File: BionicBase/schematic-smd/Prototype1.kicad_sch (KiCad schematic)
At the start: 11 parts, among them J1 Bionic_ZIF_Socket_48pin, SW1 Tact_SW, U1 TXS0108EPW, U2 TXS0108EPW, U3 TXS0108EPW, U4 TXS0108EPW, U5 TXS0108EPW

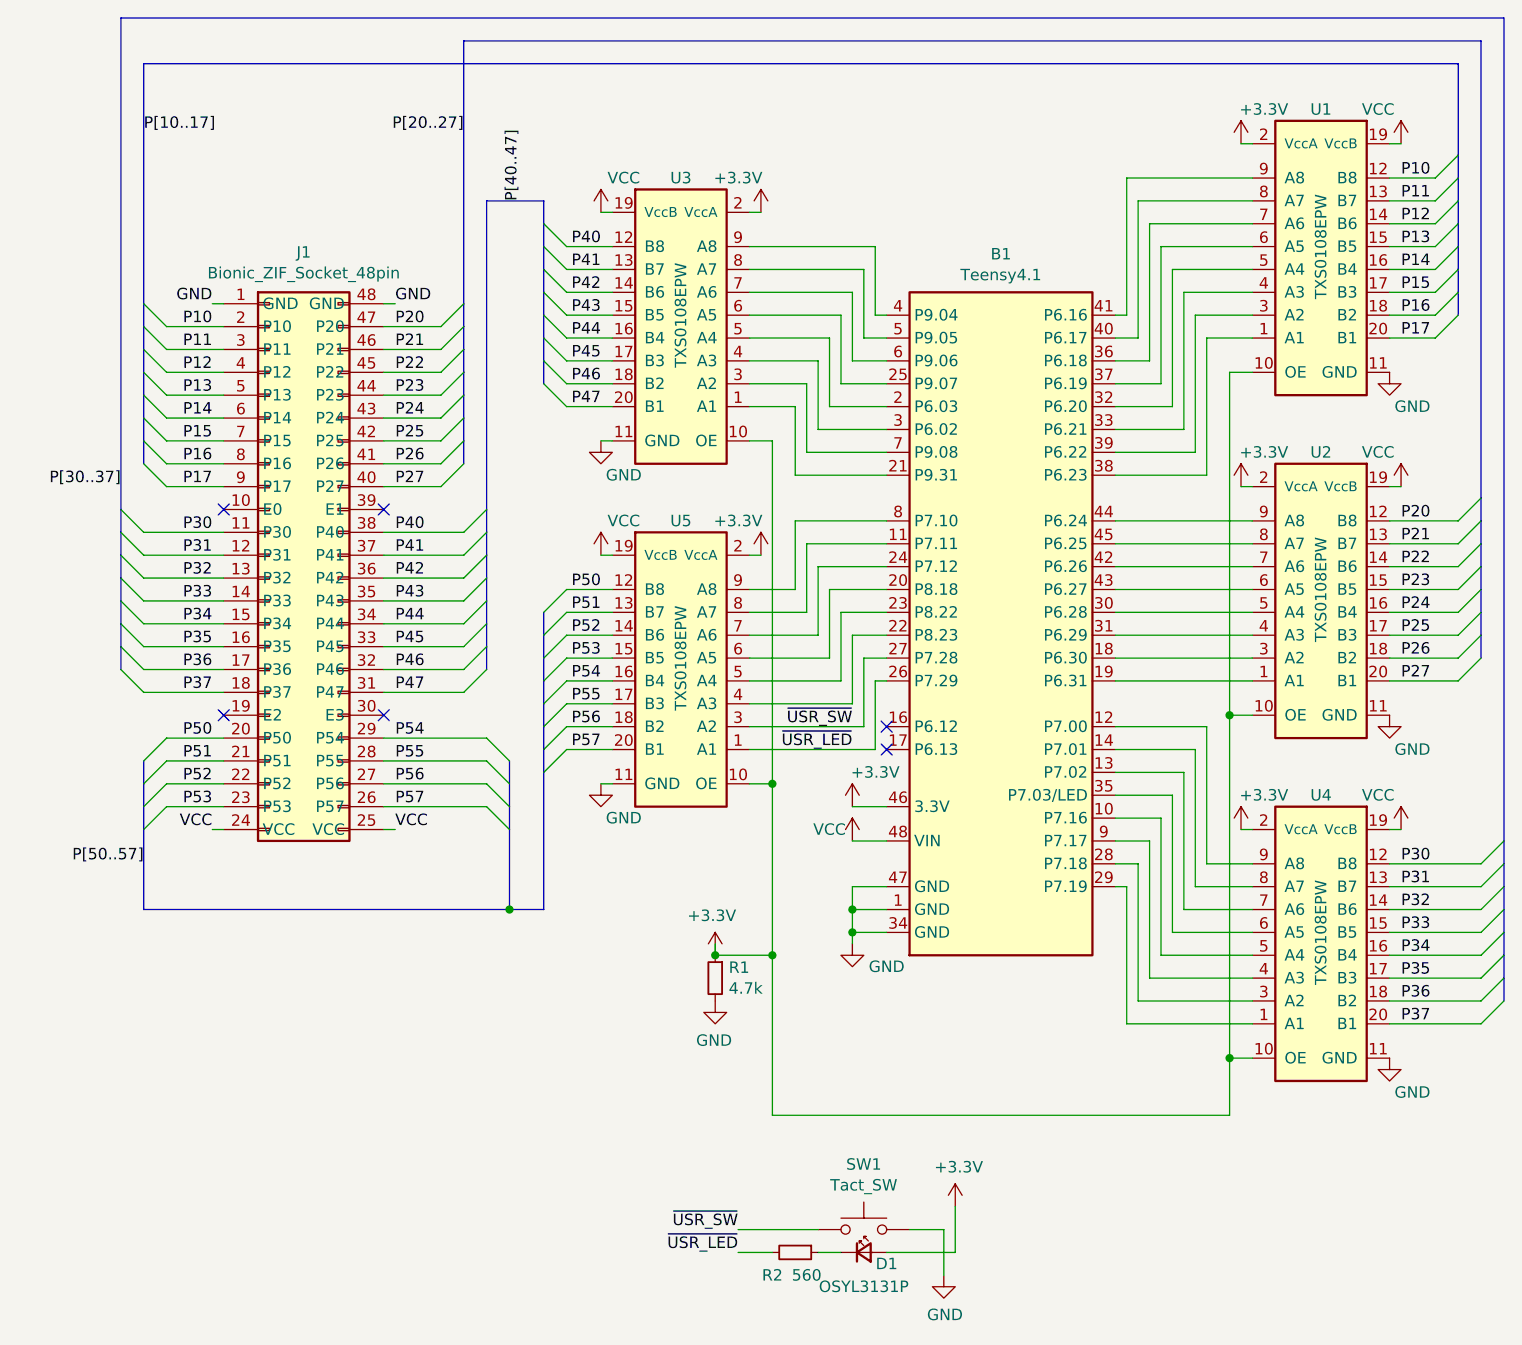
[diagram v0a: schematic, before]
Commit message: [BionicBase] Add schematics using surface mount devices
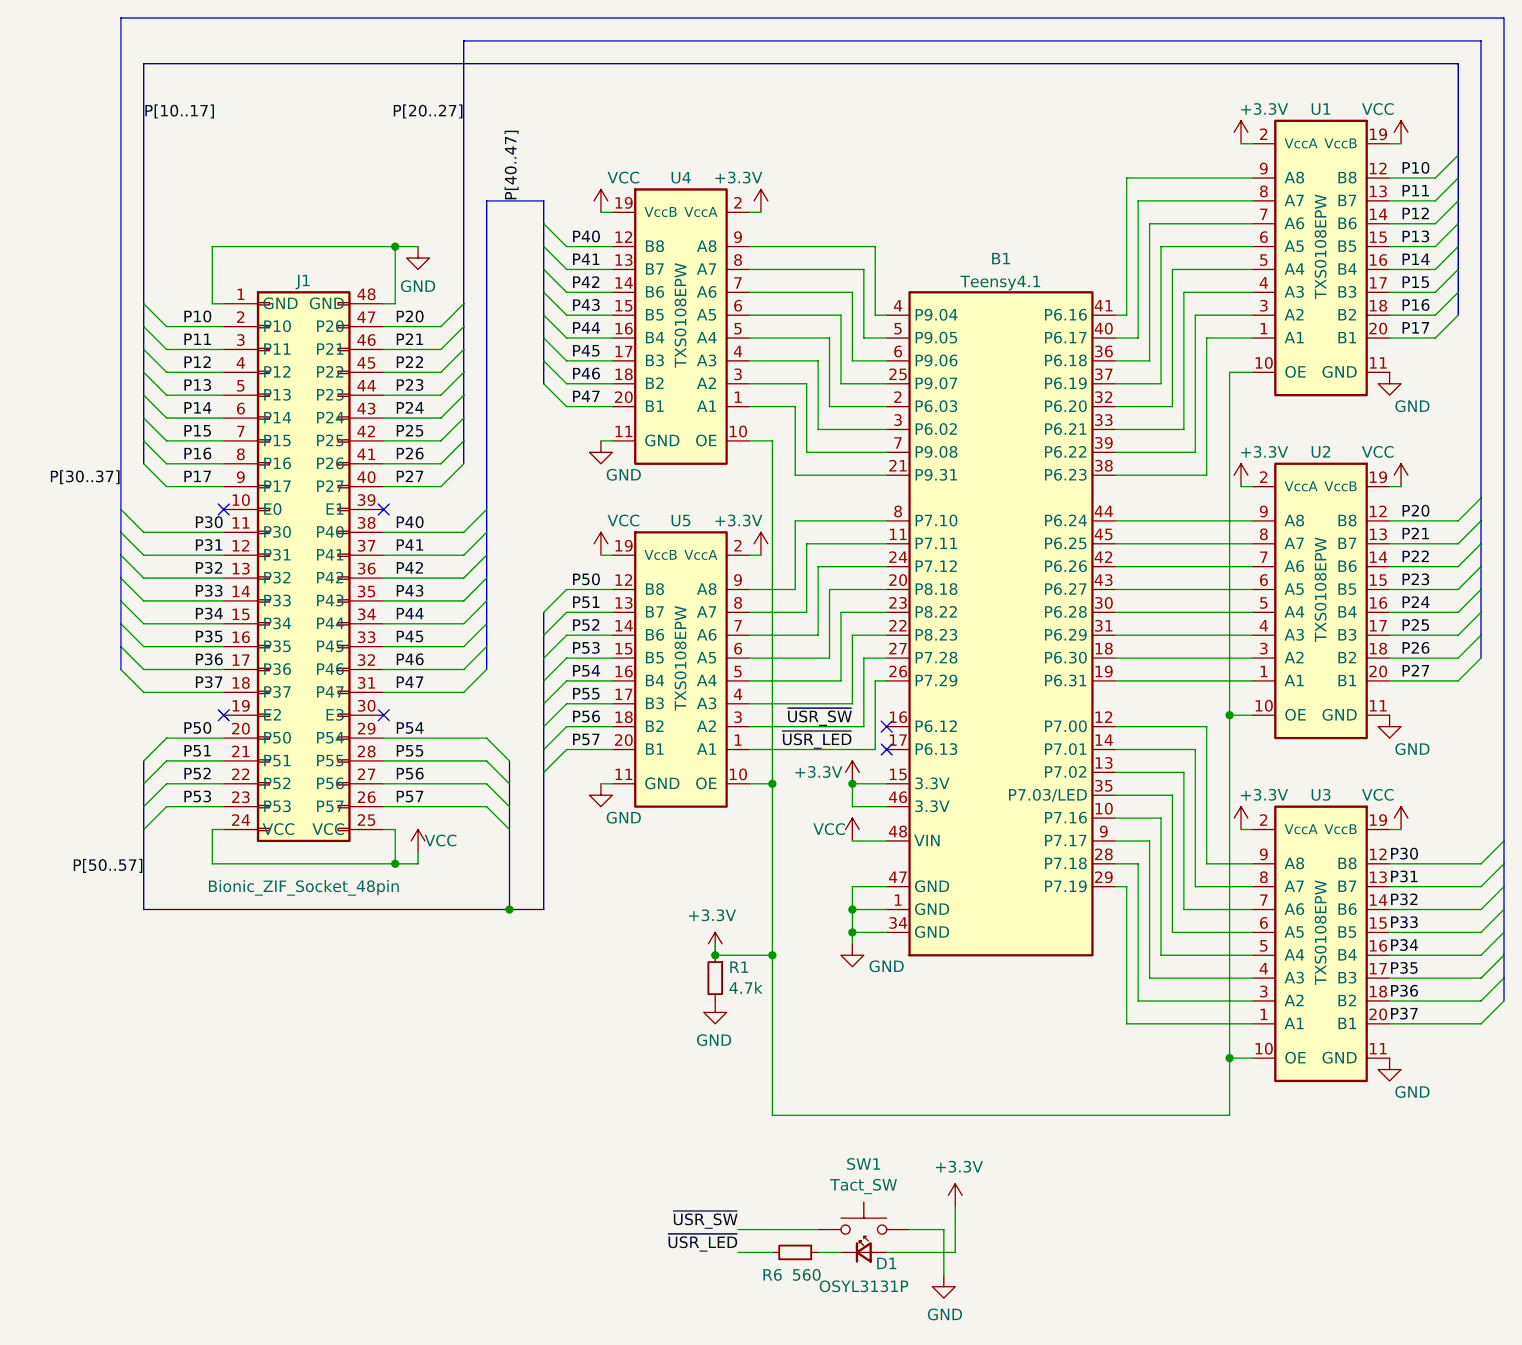
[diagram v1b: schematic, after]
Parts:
- renumbered R2 to R6
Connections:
- net P30: now also U3.12 (B8); no longer U4.12 (B8)
- net P31: now also U3.13 (B7); no longer U4.13 (B7)
- net P32: now also U3.14 (B6); no longer U4.14 (B6)
- net P33: now also U3.15 (B5); no longer U4.15 (B5)
- net P34: now also U3.16 (B4); no longer U4.16 (B4)
- net P35: now also U3.17 (B3); no longer U4.17 (B3)
- net P36: now also U3.18 (B2); no longer U4.18 (B2)
- net P37: now also U3.20 (B1); no longer U4.20 (B1)
- net P40: now also U4.12 (B8); no longer U3.12 (B8)
- net P41: now also U4.13 (B7); no longer U3.13 (B7)
- net P42: now also U4.14 (B6); no longer U3.14 (B6)
- net P43: now also U4.15 (B5); no longer U3.15 (B5)
- net P44: now also U4.16 (B4); no longer U3.16 (B4)
- net P45: now also U4.17 (B3); no longer U3.17 (B3)
- net P46: now also U4.18 (B2); no longer U3.18 (B2)
- net P47: now also U4.20 (B1); no longer U3.20 (B1)
- net at B1.10 (P7.16): now also U3.5 (A4); no longer U4.5 (A4)
- net at B1.12 (P7.00): now also U3.9 (A8); no longer U4.9 (A8)
- net at B1.13 (P7.02): now also U3.7 (A6); no longer U4.7 (A6)
- net at B1.14 (P7.01): now also U3.8 (A7); no longer U4.8 (A7)
- net at B1.2 (P6.03): now also U4.5 (A4); no longer U3.5 (A4)
- net at B1.21 (P9.31): now also U4.1 (A1); no longer U3.1 (A1)
- net at B1.25 (P9.07): now also U4.6 (A5); no longer U3.6 (A5)
- net at B1.28 (P7.18): now also U3.3 (A2); no longer U4.3 (A2)
- net at B1.29 (P7.19): now also U3.1 (A1); no longer U4.1 (A1)
- net at B1.3 (P6.02): now also U4.4 (A3); no longer U3.4 (A3)
- net at B1.35 (P7.03/LED): now also U3.6 (A5); no longer U4.6 (A5)
- net at B1.4 (P9.04): now also U4.9 (A8); no longer U3.9 (A8)
- net at B1.5 (P9.05): now also U4.8 (A7); no longer U3.8 (A7)
- net at B1.6 (P9.06): now also U4.7 (A6); no longer U3.7 (A6)
- net at B1.7 (P9.08): now also U4.3 (A2); no longer U3.3 (A2)
- net at B1.9 (P7.17): now also U3.4 (A3); no longer U4.4 (A3)
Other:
- title: BionicBase Teensy 4.1 -> BionicBase Teensy 4.1 (SMD)

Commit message: [BionicBase] Add DC-DC Converter for +15V
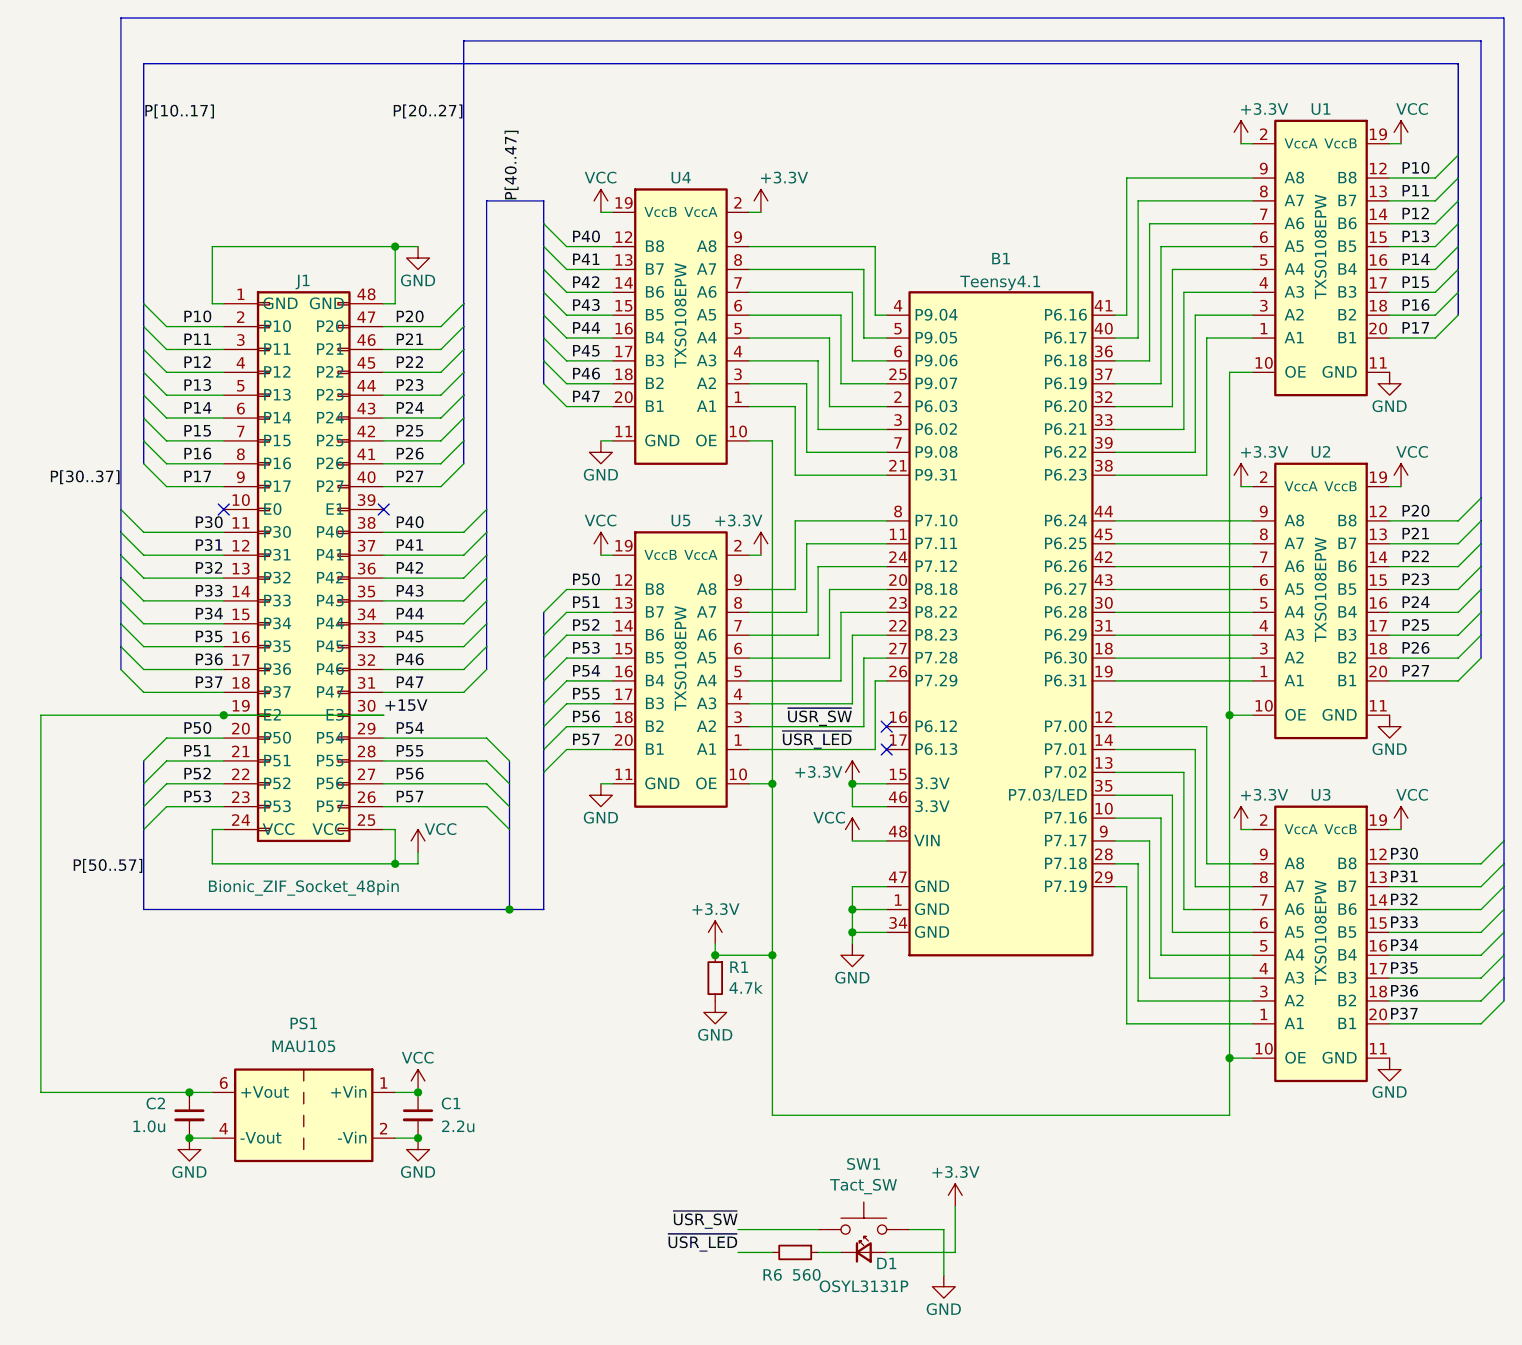
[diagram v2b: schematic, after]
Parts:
- added C1: 2.2u, Capacitor_SMD:C_0603_1608Metric_Pad1.08x0.95mm_HandSolder, symbol Device:C_Small
- added C2: 1.0u, Capacitor_SMD:C_0603_1608Metric_Pad1.08x0.95mm_HandSolder, symbol Device:C_Small
- added PS1: MAU105, 0-LocalLibrary:Converter_DCDC_Minmax_MAU100_THT, symbol 0-LocalLibrary:MAU105
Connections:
- net GND: now also C1.2, C2.2, PS1.2 (-Vin), PS1.4 (-Vout)
- net VCC: now also C1.1, PS1.1 (+Vin)
- net +15V: now reaches J1.19 (E2)
- net +15V: now also J1.30 (E3), C2.1, PS1.6 (+Vout)
- net +3V3 renamed +3.3V
- no-connect marks 6 -> 4
